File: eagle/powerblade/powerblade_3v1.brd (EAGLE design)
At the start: 25.4 x 25.4 mm, 79 parts, among them J1 JTAG_14PIN_IDC-NL, J2 AC_INF2, J4 TC2030-JLINK-NL, Q1 2N7002, Q4 2SK1829, U1 TPS62122, U2 MCP6V3, U3 MSP430FR5738, U4 NRF51822QF, U6 MAX9910, U7 OPA2369, X1 16MHz, X3 32.768kHz, Y1 UREACH_XTEND

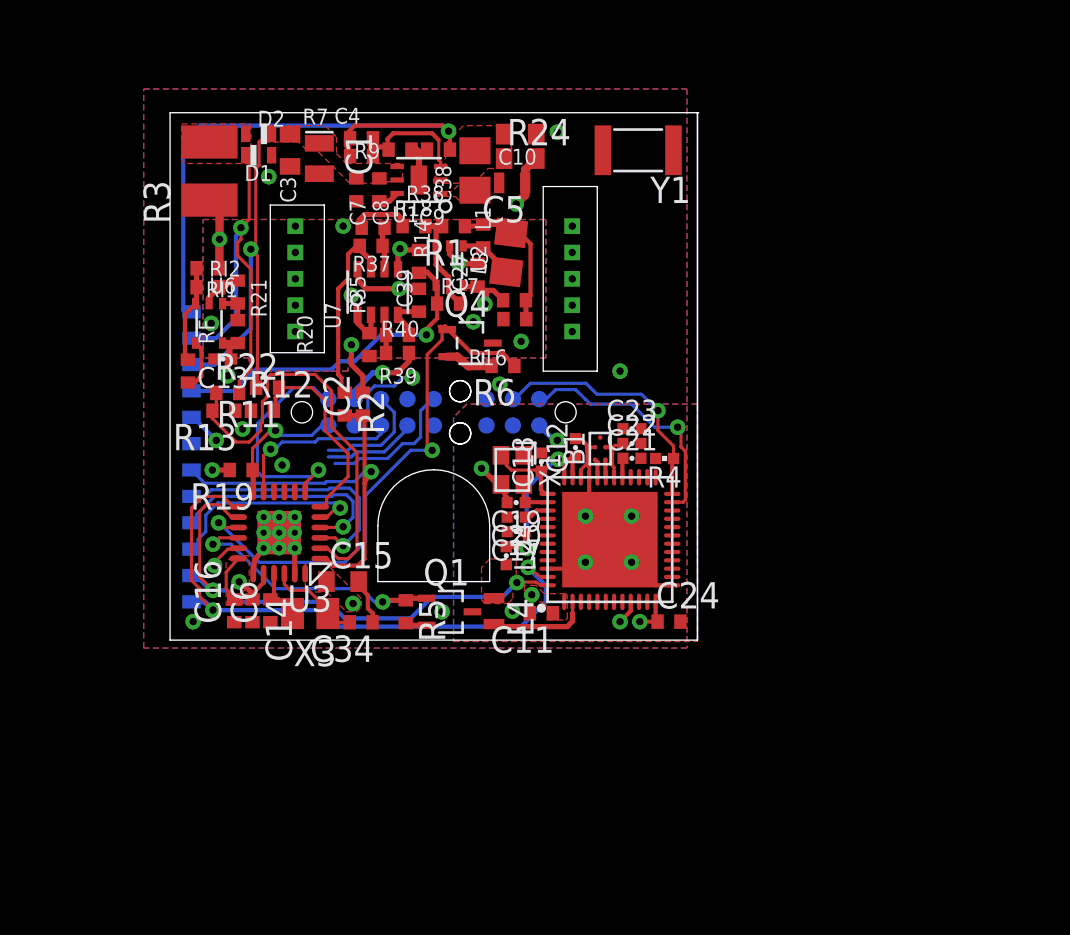
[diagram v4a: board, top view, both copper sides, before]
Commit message: finished airwires but still a few errors
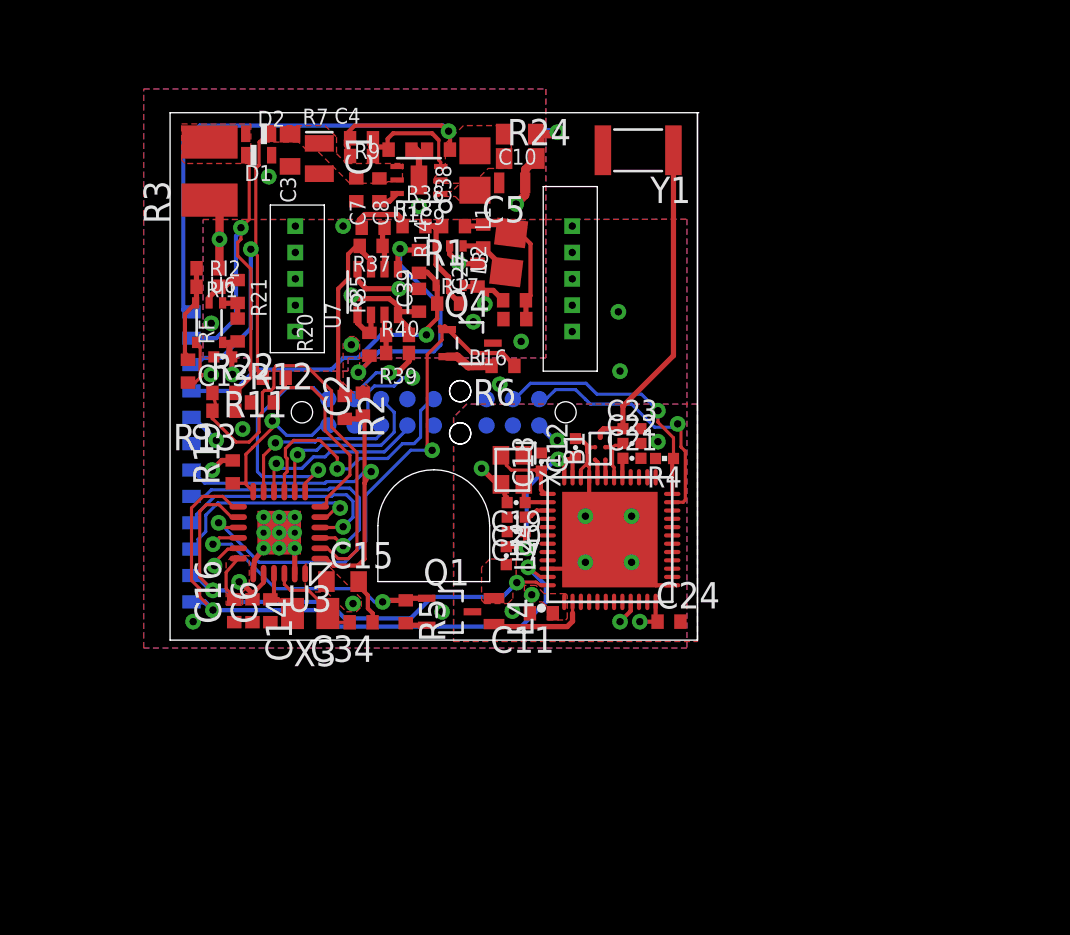
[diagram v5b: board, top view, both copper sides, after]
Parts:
- moved R11 0.57 mm to (-7.68, -4.76)
- moved R19 0.42 mm to (-9.68, -9.30), turned to 90 degrees
- moved R12 0.40 mm to (-8.26, -5.95)
- moved R22 0.19 mm to (-10.1, -5.49)
- moved R2 0.16 mm to (-4.29, -6.19)
- moved C13 0.10 mm to (-10.2, -3.76)
- moved R20 0.08 mm to (-9.45, -2.46)
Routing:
- net N$4: track 0.00 -> 15.8 mm
- net V_SENSE: track 12.7 -> 26.6 mm, vias 1 -> 2
- net N$67: track 1.96 -> 12.9 mm, vias 1 -> 2
- net GND: track 15.5 -> 23.3 mm, vias 8 -> 10
- net TMS: track 6.79 -> 12.5 mm, vias 0 -> 1
- net TCK: track 4.53 -> 8.75 mm, vias 0 -> 1
- net TDI: track 5.39 -> 8.79 mm, vias 0 -> 1
- net RST: track 6.39 -> 7.90 mm
- net ZC_LOW: track 20.8 -> 21.4 mm
- net GND3: track 11.7 -> 12.3 mm
- net GND2: vias 6 -> 7

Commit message: updated board
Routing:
- net GND: vias 10 -> 11
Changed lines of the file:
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@@
 <wire x1="5.953125" y1="7.064375" x2="4.841875" y2="7.064375" width="0.4064" layer="16"/>
 <wire x1="4.841875" y1="7.064375" x2="4.7625" y2="6.985" width="0.4064" layer="16"/>
+<via x="11.58875" y="-5.159375" extent="1-16" drill="0.3556"/>
 </signal>
 <signal name="N$10">
